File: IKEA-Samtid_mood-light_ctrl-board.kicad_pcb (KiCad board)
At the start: 2 copper layers, 41.3 x 15.5 mm, 15 parts, among them IC1 ATMEGA168PA-M, P1 FTDI, P3.2 B-to-B-1B, P4.2 B-to-B-2B, SW1 ENTER, SW2 MODE, X1 CSTCE16M0V53-R0

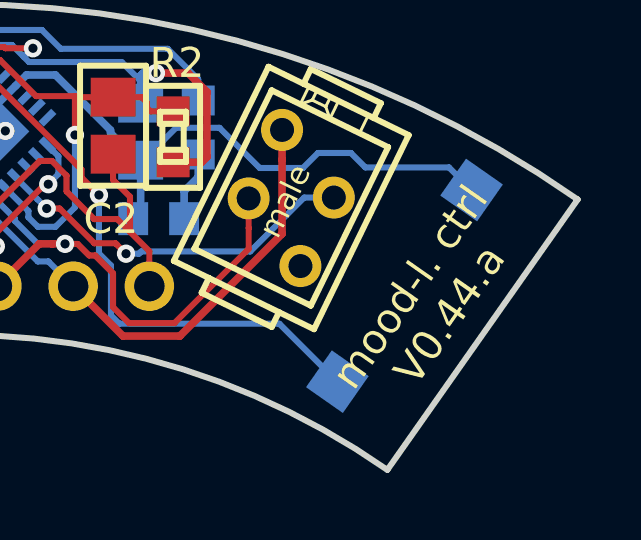
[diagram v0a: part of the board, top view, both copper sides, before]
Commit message: Added Deans mini-T power connector. It fits! Might be ready now.
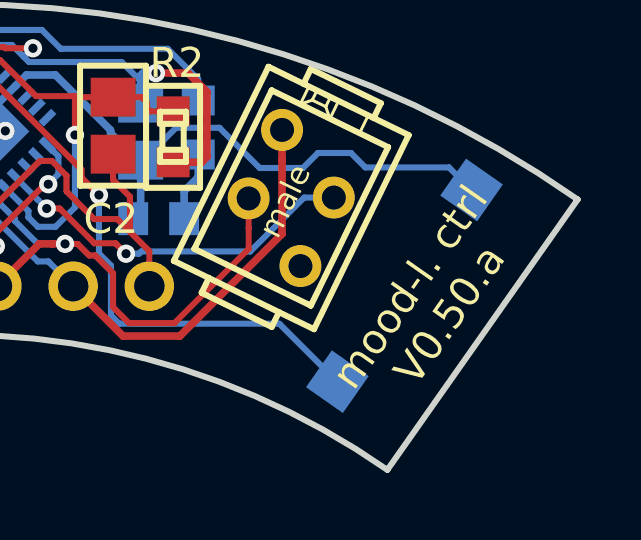
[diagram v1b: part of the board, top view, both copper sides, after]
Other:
- board text added: "mood-l. ctrl V0.50.a"
- board text removed: "mood-l. ctrl V0.44.a"
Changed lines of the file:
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@@
-(kicad_pcb (version 4) (host pcbnew "(2015-02-06 BZR 5410)-product")
+(kicad_pcb (version 4) (host pcbnew "(2015-02-11 BZR 5414)-product")
   (general
     (links 39)
@@
   (title_block
     (title IKEA-Samtid_mood-light_ctrl-board)
-    (date "Fri 06 Feb 2015")
-    (rev 0.44.a)
+    (date "Thu 12 Feb 2015")
+    (rev 0.50.a)
     (company "2015 - blog.spitzenpfeil.org")
   )
@@
     (34 B.Paste user)
     (35 F.Paste user)
-    (36 B.SilkS user hide)
+    (36 B.SilkS user)
     (37 F.SilkS user)
-    (38 B.Mask user hide)
-    (39 F.Mask user hide)
-    (40 Dwgs.User user hide)
-    (41 Cmts.User user hide)
-    (42 Eco1.User user hide)
+    (38 B.Mask user)
+    (39 F.Mask user)
+    (40 Dwgs.User user)
+    (41 Cmts.User user)
+    (42 Eco1.User user)
     (44 Edge.Cuts user)
   )
   (setup
-    (last_trace_width 0.2032)
+    (last_trace_width 0.4064)
     (user_trace_width 0.2032)
     (user_trace_width 0.254)
@@
     (visible_elements FFFFFF7F)
     (pcbplotparams
-      (layerselection 0x010f0_80000001)
+      (layerselection 0x017fc_80000001)
       (usegerberextensions true)
       (excludeedgelayer true)
@@
     (effects (font (size 1 1) (thickness 0.2)))
   )
-  (gr_text "mood-l. ctrl\nV0.44.a" (at 165.83 97.13 55) (layer F.SilkS)
+  (gr_text "mood-l. ctrl\nV0.50.a" (at 165.83 97.13 55) (layer F.SilkS)
     (effects (font (size 1 1) (thickness 0.2)))
   )

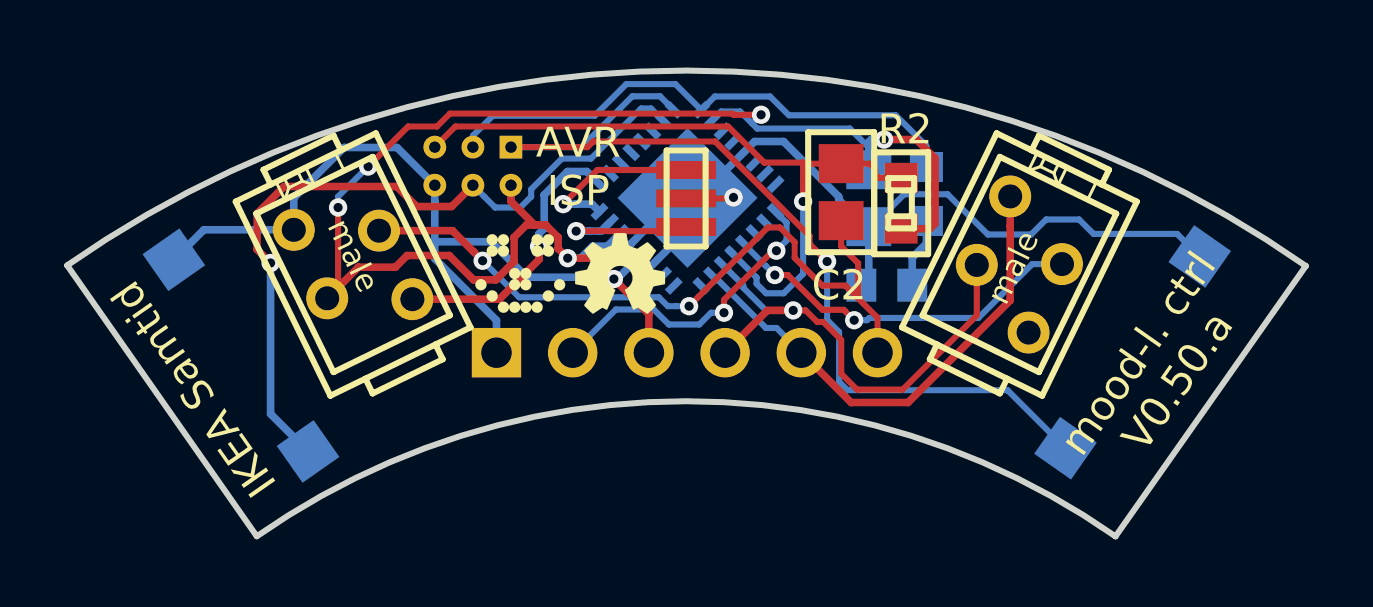
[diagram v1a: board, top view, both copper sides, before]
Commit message: Added solder-bridge to enable/disable remote programming via BT.
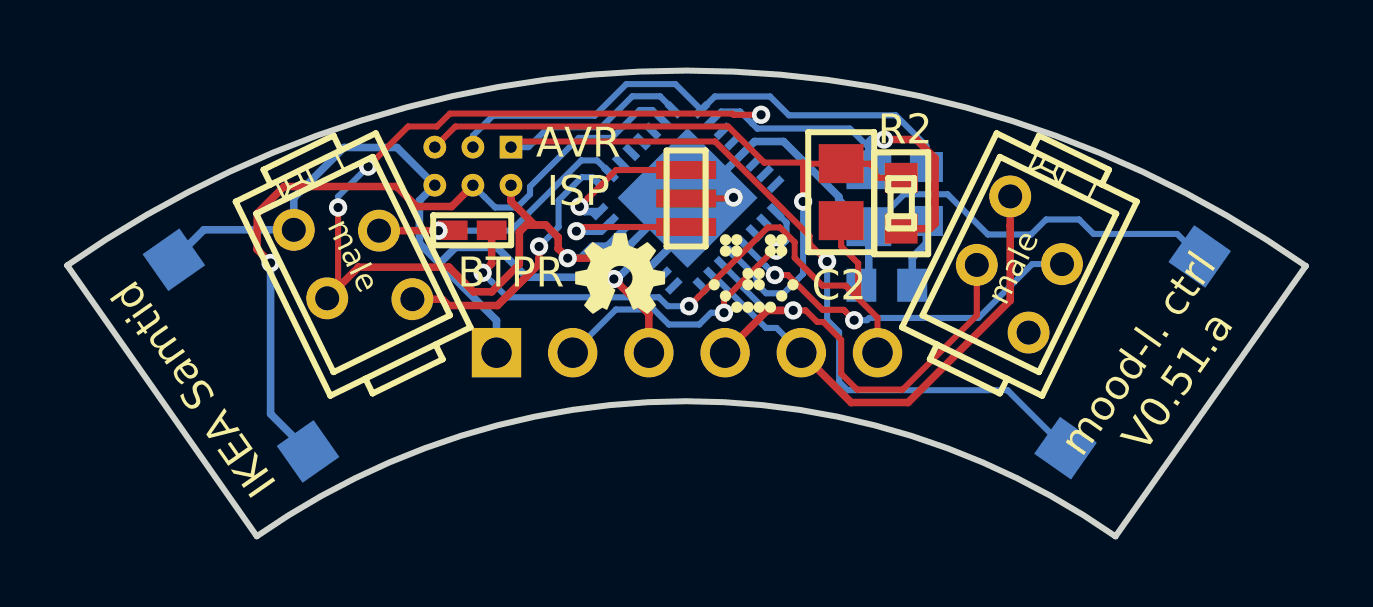
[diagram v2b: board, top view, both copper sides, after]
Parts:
- added JP2: BT-PROG_EN, my_parts:MADW__SMD-solder-bridge-narrow, F.Cu at (143.0, 92.6)
- moved LOGO1 7.78 mm to (152.3, 94.0)
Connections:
- IC1 pad 10: (no net) -> /STATE.B
- P3.2 pad 2: /DTR.B -> /STATE.B
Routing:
- net /STATE.B: track 0.00 -> 10.2 mm, vias 0 -> 1
- net /DTR.B: track 24.9 -> 22.0 mm
- net /XTAL2: track 5.88 -> 4.79 mm
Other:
- board text added: "BTPR"
- board text added: "mood-l. ctrl V0.51.a"
- board text removed: "mood-l. ctrl V0.50.a"

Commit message: Replaced BT solder bridge with 1.27mm jumper.
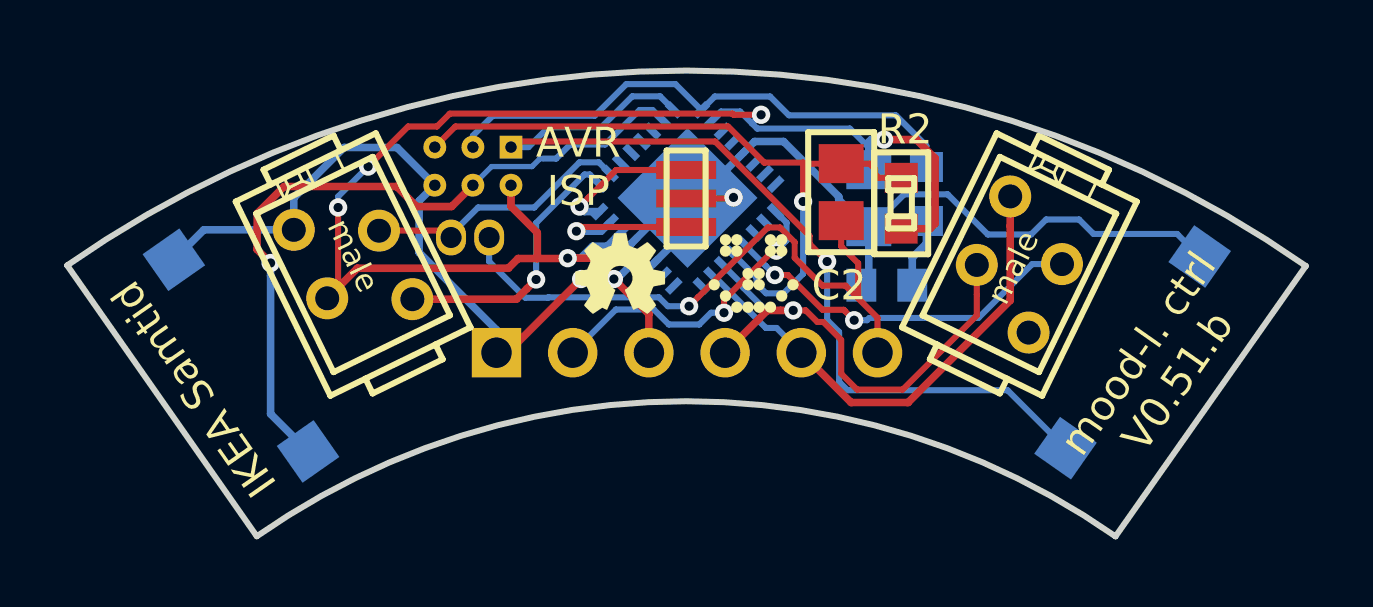
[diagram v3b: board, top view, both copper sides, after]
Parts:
- JP2: footprint my_parts:MADW__SMD-solder-bridge-narrow -> SIL-2-1.27mm; moved to B.Cu
- moved JP2 0.25 mm to (142.9, 92.8)
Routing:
- net /GND.B: track 57.0 -> 55.5 mm, vias 1 -> 2
- net /VCC.B: track 52.8 -> 51.7 mm
- net /STATE.B: track 10.2 -> 9.09 mm, vias 1 -> 0
- net /DTR.B: track 22.0 -> 21.2 mm, vias 2 -> 1
- net /MOSI: track 25.1 -> 24.4 mm
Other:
- rule trace_min: 0.2032 -> 0.1524
- board text added: "BT"
- board text added: "mood-l. ctrl V0.51.b"
- board text removed: "BTPR"
- board text removed: "GND"
- board text removed: "mood-l. ctrl V0.51.a"

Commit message: Layout tweaks.
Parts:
- IC1: footprint SMD_Packages:QFN-32-1EP -> Housings_DFN_QFN:QFN-32-1EP_5x5mm_Pitch0.5mm
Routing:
- net /GND.B: track 55.5 -> 56.8 mm
- net /XTAL2: track 4.79 -> 5.95 mm
- net /LEDS.B: track 9.19 -> 9.77 mm
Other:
- rule pad_to_mask_clearance: 0 -> 0.025
- board text added: "mood-l. ctrl V0.51.c"
- board text removed: "mood-l. ctrl V0.51.b"

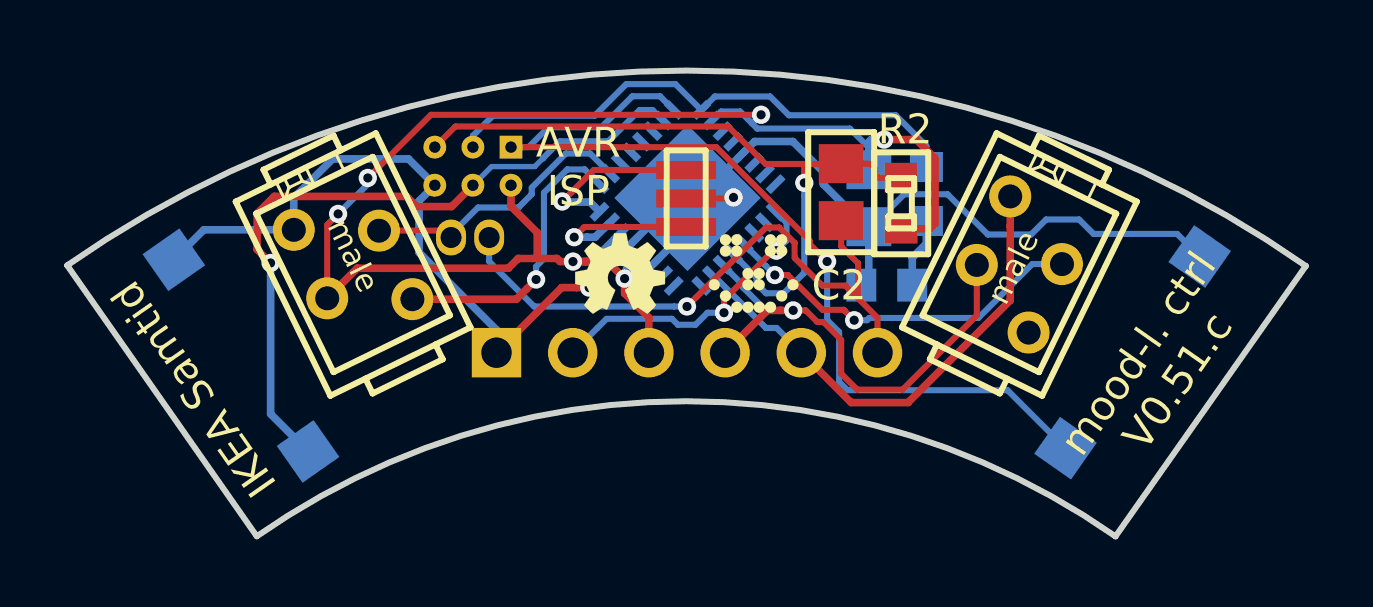
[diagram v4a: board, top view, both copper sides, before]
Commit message: Changed BT jumper to 2.00mm one. Much easier to get.
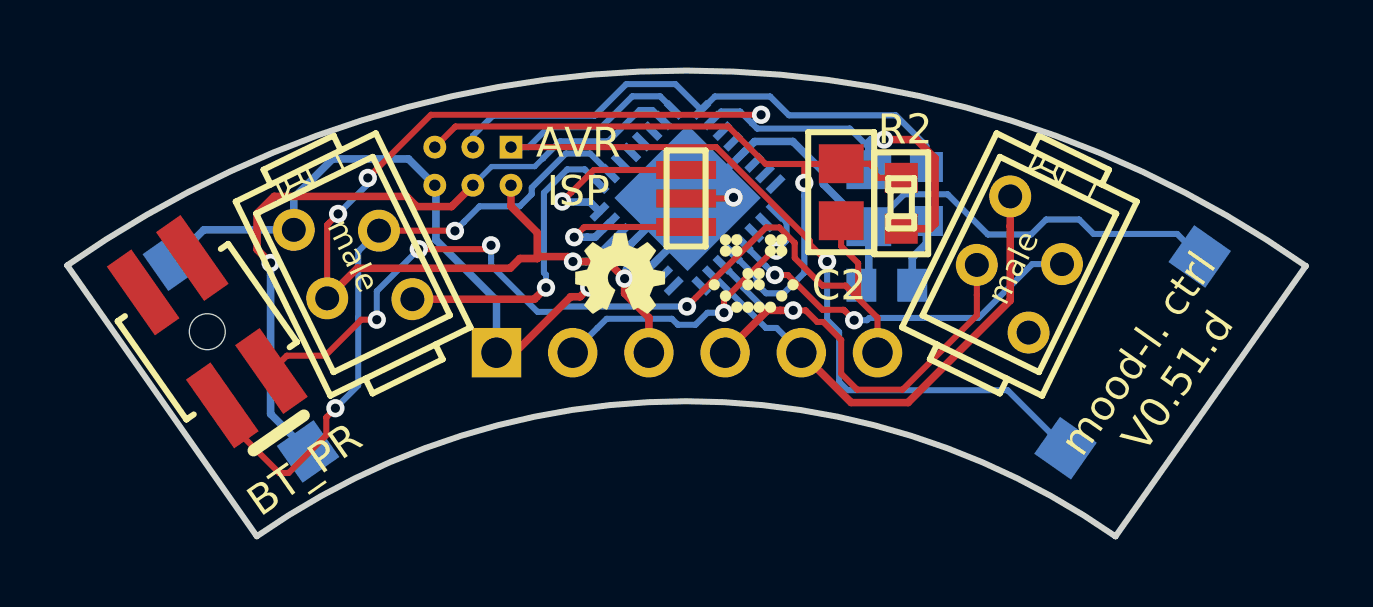
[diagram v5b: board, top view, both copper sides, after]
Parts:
- JP2: footprint SIL-2-1.27mm -> DIL-Headers:DIL-2-2.00mm_male_vert_SMD_PH2M15-2XX-U; moved to F.Cu
- moved JP2 9.31 mm to (134.1, 95.9), turned to 35 degrees
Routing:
- net /STATE.B: track 9.46 -> 21.9 mm, vias 0 -> 2
- net /DTR.B: track 21.0 -> 30.5 mm, vias 1 -> 4
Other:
- board text added: "BT_PR"
- board text added: "GND"
- board text added: "mood-l. ctrl V0.51.d"
- board text removed: "BT"
- board text removed: "IKEA Samtid"
- board text removed: "mood-l. ctrl V0.51.c"

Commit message: Made ctrl-board some 0.1mm wider (radially) --> no traces near edge.
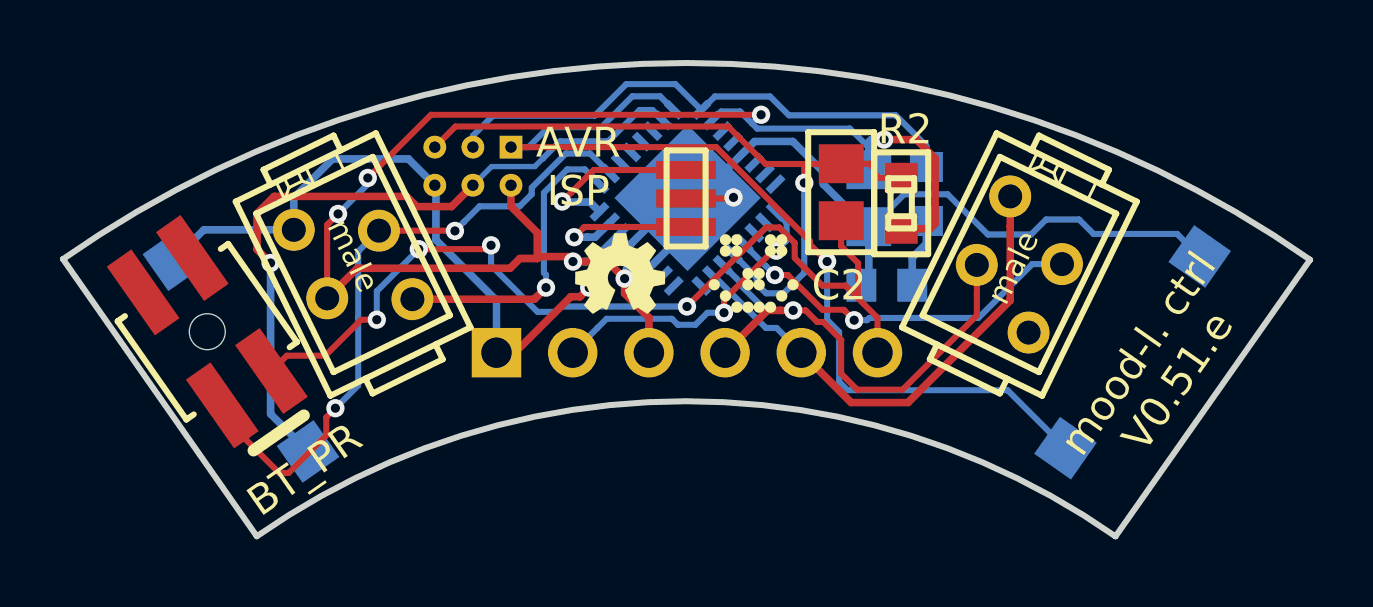
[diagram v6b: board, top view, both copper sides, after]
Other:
- board size 41.3 x 15.5 mm -> 41.6 x 15.8 mm
- board text added: "mood-l. ctrl V0.51.e"
- board text removed: "mood-l. ctrl V0.51.d"

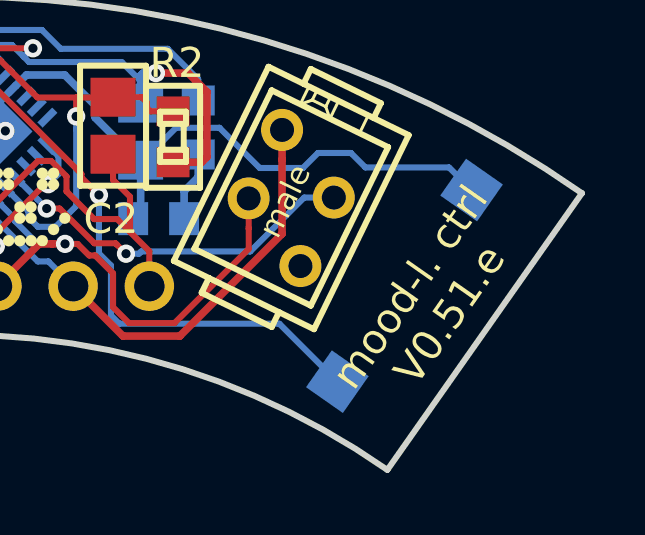
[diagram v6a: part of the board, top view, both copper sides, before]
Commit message: Added alternative footprint for power input (5-pin Molex KK).
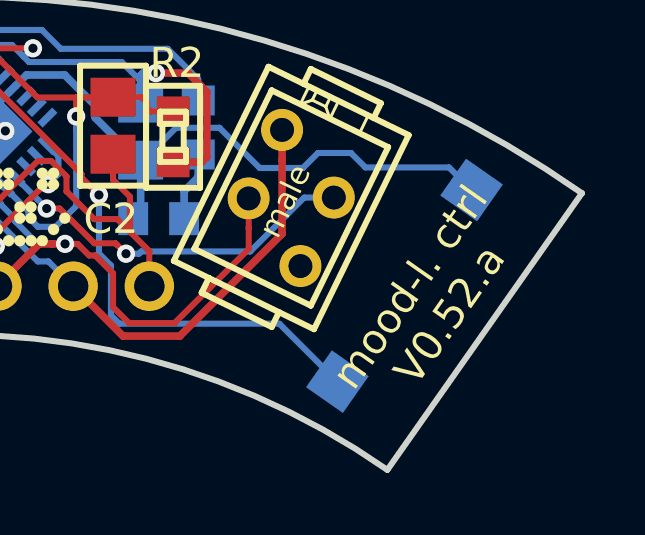
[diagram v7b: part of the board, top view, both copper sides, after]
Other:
- board text added: "mood-l. ctrl V0.52.a"
- board text removed: "mood-l. ctrl V0.51.e"

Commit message: Updated BOM file + other very minor stuff.
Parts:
- renumbered D65 to LED65
